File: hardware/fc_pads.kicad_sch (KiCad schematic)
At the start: 41 parts, among them J15 5V, J16 5V, J17 5V, J18 5V, J19 5V, J20 5V, J21 5V, J22 5V, J23 5V, J24 5V, J25 5V, J26 5V, J27 5V, J28 5V, J29 5V, J30 5V, J31 5V, J32 5V, J33 5V, J34 5V, J35 5V, J37 5V, J38 5V, J39 5V, J40 5V, J41 5V, J42 5V, J43 5V, J44 5V, J45 5V, J46 5V, J47 5V, J48 5V, J49 5V, J50 5V, J51 5V, J52 5V, J53 5V, J54 5V, J55 5V, U12 SM06B-SRSS-TB(LF)(SN)

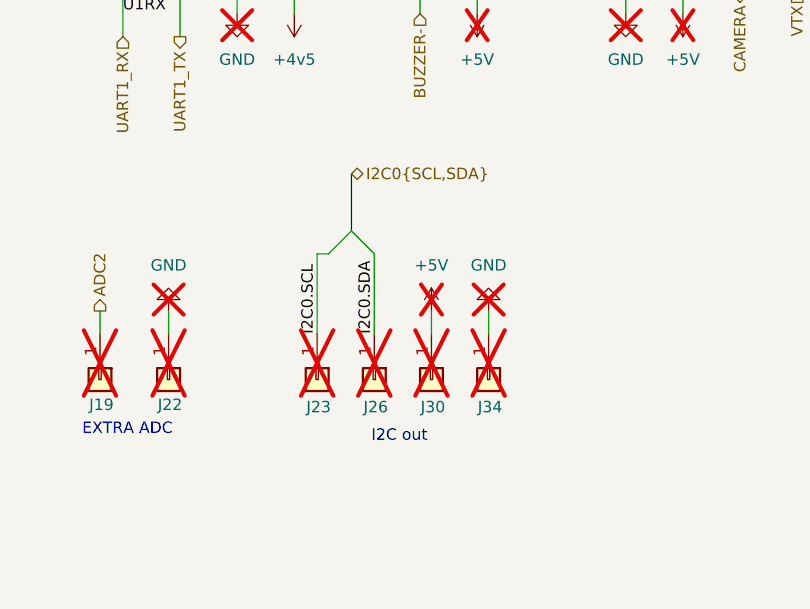
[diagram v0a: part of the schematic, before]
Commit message: One board: the flight controller is the OpenFC-Core module
The core sheets, the second board project and the multiboard split are
gone; OpenDrone-Core sits on the root schematic as J1 and its land is on
the board at (78.0, 61.65) with the existing routing kept. Board settings
and 2 oz rules carried over from the Base project. Docs updated.

Co-Authored-By: Claude Fable 5 <noreply@anthropic.com>
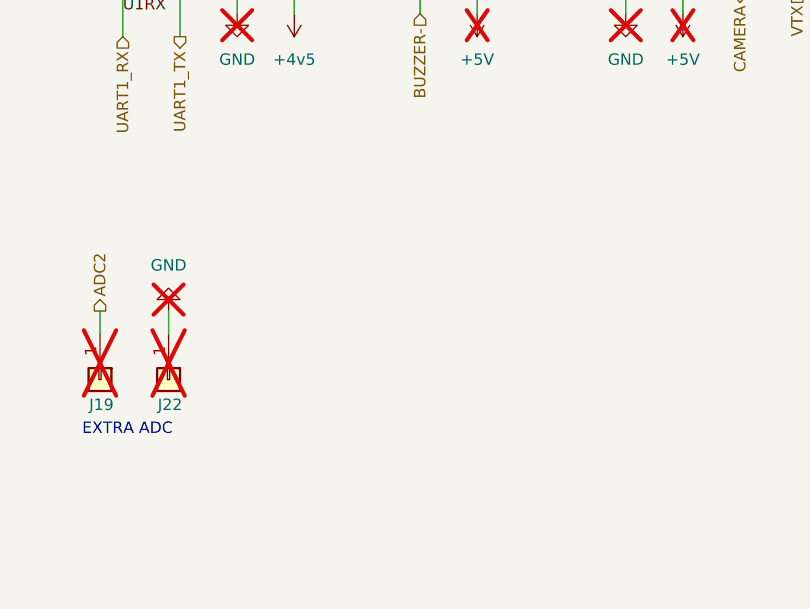
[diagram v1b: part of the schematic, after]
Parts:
- removed J23, J26, J30, J34: 5V, lib:small_pad, symbol Connector_Generic:Conn_01x01
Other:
- note removed: "I2C out"
